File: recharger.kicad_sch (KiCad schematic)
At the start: 22 parts, among them J1 USB_C_Receptacle_USB2.0_14P, J3 Conn_01x03, U2 BQ25886RGE, U3 TPD2EUSB30

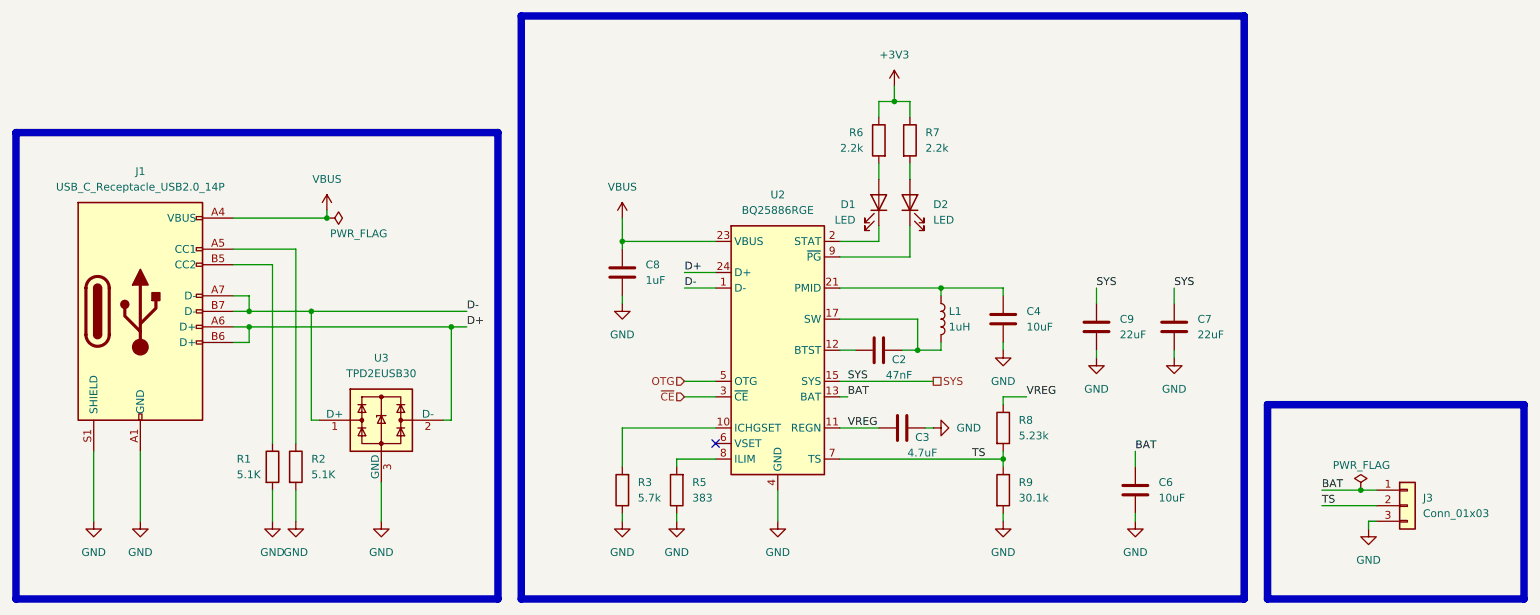
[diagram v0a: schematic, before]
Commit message: update schematic
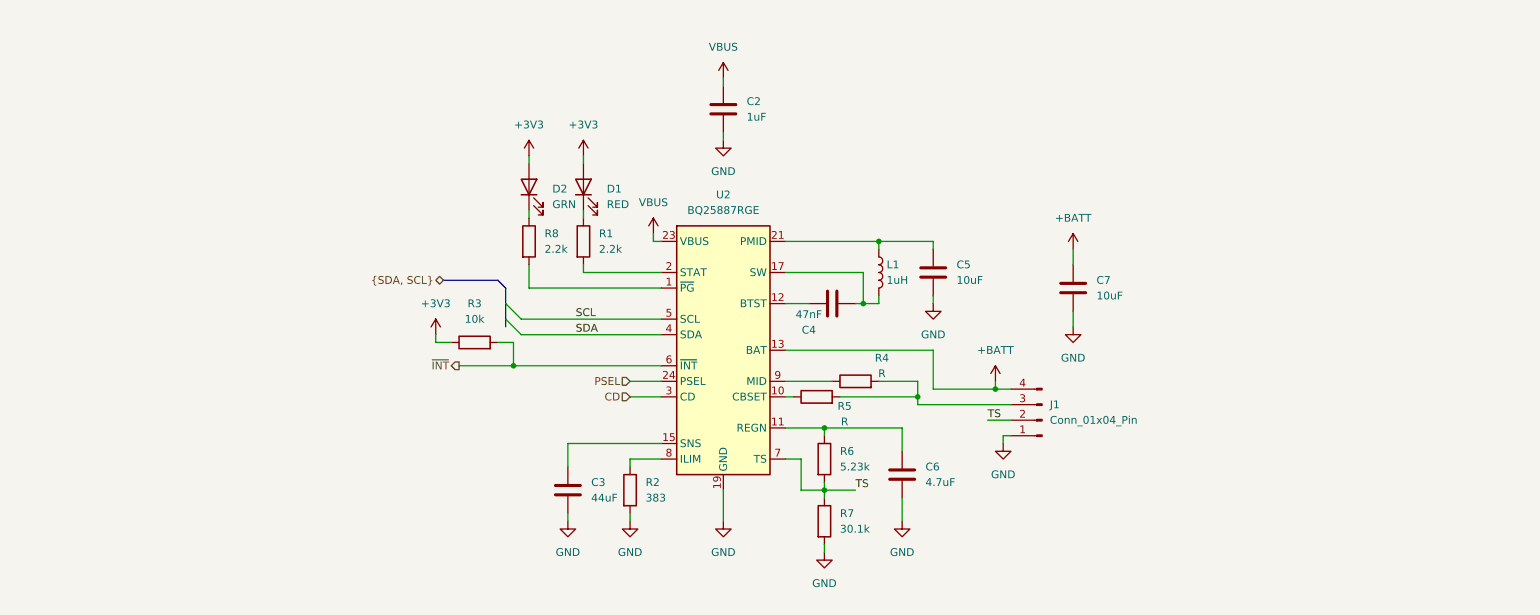
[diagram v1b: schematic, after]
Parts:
- removed C8: 1uF, Capacitor_SMD:C_0402_1005Metric, symbol Device:C
- removed C9: 22uF, Capacitor_SMD:C_1210_3225Metric, symbol Device:C
- removed J1: USB_C_Receptacle_USB2.0_14P, Connector_USB:USB_C_Receptacle_G-Switch_GT-USB-7010ASV, symbol Connector:USB_C_Receptacle_USB2.0_14P
- removed J3: Conn_01x03, symbol Connector_Generic:Conn_01x03
- removed R9: 30.1k, symbol Device:R
- removed U2: BQ25886RGE, Package_DFN_QFN:Texas_RGE0024H_VQFN-24-1EP_4x4mm_P0.5mm_EP2.7x2.7mm, symbol Battery_Management:BQ25886RGE
- removed U3: TPD2EUSB30, Package_TO_SOT_SMD:Texas_DRT-3, symbol Power_Protection:TPD2EUSB30
- added C5: 10uF, symbol Device:C
- added J1: Conn_01x04_Pin, symbol Connector:Conn_01x04_Pin
- added R4: R, symbol Device:R
- added U2: BQ25887RGE, Package_DFN_QFN:Texas_RGE0024H_VQFN-24-1EP_4x4mm_P0.5mm_EP2.7x2.7mm, symbol Battery_Management:BQ25887RGE
- C2: value 47nF -> 1uF; footprint Capacitor_SMD:C_0402_1005Metric -> (none)
- C3: value 4.7uF -> 44uF; footprint Capacitor_SMD:C_0603_1608Metric -> (none)
- C4: value 10uF -> 47nF; footprint Capacitor_SMD:C_0603_1608Metric -> (none)
- C6: value 10uF -> 4.7uF; footprint Capacitor_SMD:C_0805_2012Metric -> (none)
- C7: value 22uF -> 10uF; footprint Capacitor_SMD:C_1210_3225Metric -> (none)
- D1: value LED -> RED
- D2: value LED -> GRN
- L1: footprint Inductor_SMD:L_1008_2520Metric -> (none)
- R1: value 5.1K -> 2.2k; footprint Resistor_SMD:R_0805_2012Metric -> (none); LCSC C27834 -> (none)
- R2: value 5.1K -> 383; footprint Resistor_SMD:R_0805_2012Metric -> (none); LCSC C27834 -> (none)
- R3: value 5.7k -> 10k
- R5: value 383 -> R
- R6: value 2.2k -> 5.23k
- R7: value 2.2k -> 30.1k
- R8: value 5.23k -> 2.2k
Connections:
- net +3V3: now also D1.2 (A), D2.2 (A), R3.1; no longer R6.1, R7.1
- net GND: now also C2.2, R7.2, C5.2, J1.1 (Pin_1), U2.19 (GND), U2.20 (GND), U2.25 (GND); no longer C4.2, R1.2, R3.1, R5.1
- net TS: now also R6.2, R7.1, J1.2 (Pin_2), U2.7 (TS); no longer R8.2
- net VBUS: now also C2.1, U2.23 (VBUS)
- net ~{INT}: now reaches R3.2
- net ~{INT}: now also U2.6 (~{INT})
- net at L1.2: now also C4.1, U2.17 (SW), U2.18 (SW); no longer C2.2
- net at D1.1 (K): now also R1.1
- net at L1.1: now also C5.1, U2.21 (PMID), U2.22 (PMID); no longer C4.1
- net at R5.2: now also J1.3 (Pin_3), R4.2
- net at D2.1 (K): now also R8.1
- net at R2.1: now also U2.8 (ILIM)
- net BAT: no longer names the net of C6.1
- net BAT: now also R6.1, U2.11 (REGN)
- net SYS renamed +BATT
- net +BATT: now also J1.4 (Pin_4), U2.13 (BAT), U2.14 (BAT)
- net VREG: no longer names the net of C3.1
- net VREG: now also U2.15 (SNS), U2.16 (SNS); no longer R8.1
- new net: R1.2, U2.2 (STAT)
- new net: R8.2, U2.1 (~{PG})
- new net: R5.1, U2.10 (CBSET)
- new net: C4.2, U2.12 (BTST)
- new net: R4.1, U2.9 (MID)
- new net CD: U2.3 (CD)
- new net PSEL: U2.24 (PSEL)
- new net SCL: U2.5 (SCL)
- new net SDA: U2.4 (SDA)
- no-connect marks 1 -> 0

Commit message: improve design
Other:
- title: (none) -> Dropbot
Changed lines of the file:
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@@
 	(generator_version "10.0")
 	(paper "A4")
+	(title_block
+		(title "Dropbot")
+	)
 	(junction
 		(at 186.69 105.41)

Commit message: moving on routing
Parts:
- added C12: 22uF, Capacitor_SMD:C_1206_3216Metric, symbol Device:C
- C2, C4, C6: footprint (none) -> Capacitor_SMD:C_0603_1608Metric
- C3: value 44uF -> 22uF; footprint (none) -> Capacitor_SMD:C_1206_3216Metric
- C5: footprint (none) -> Capacitor_SMD:C_1206_3216Metric
- C7: footprint (none) -> Capacitor_SMD:C_0805_2012Metric
- D1, D2: footprint (none) -> LED_SMD:LED_0603_1608Metric
- J1: value Conn_01x04_Pin -> Battery Connector; footprint (none) -> Connector_JST:JST_PH_S4B-PH-K_1x04_P2.00mm_Horizontal
- L1: footprint (none) -> Inductor_SMD:L_1008_2520Metric
- R1, R3, R6, R7, R8: footprint (none) -> Resistor_SMD:R_0603_1608Metric
- R2: value 383 -> 1.1K; footprint (none) -> Resistor_SMD:R_0603_1608Metric
- R4: value R -> 300; footprint (none) -> Resistor_SMD:R_0603_1608Metric
- R5: footprint (none) -> Resistor_SMD:R_2512_6332Metric
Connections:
- net +3V3: no longer D1.2 (A), D2.2 (A)
- net GND: now also C12.2
- net at C3.1, U2.15 (SNS), U2.16 (SNS): now also C12.1
- net REGN: now reaches C6.1, R6.1, U2.11 (REGN)
- net REGN: now also D1.2 (A), D2.2 (A)
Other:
- moved on the sheet: C7

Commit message: update PCB
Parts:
- J1: footprint Connector_JST:JST_PH_S4B-PH-K_1x04_P2.00mm_Horizontal -> Connector_JST:JST_PH_S4B-PH-SM4-TB_1x04-1MP_P2.00mm_Horizontal
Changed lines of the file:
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@@
 			)
 		)
-		(property "Footprint" "Connector_JST:JST_PH_S4B-PH-K_1x04_P2.00mm_Horizontal"
+		(property "Footprint" "Connector_JST:JST_PH_S4B-PH-SM4-TB_1x04-1MP_P2.00mm_Horizontal"
 			(at 194.31 110.49 0)
 			(hide yes)

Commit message: more on layout
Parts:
- R5: value R -> 10
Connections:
- net CBSET_PIN: now reaches J1.3 (Pin_3), R4.2, R5.2
- net CBSET_IN: now reaches R5.1, U2.10 (CBSET)
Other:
- moved on the sheet: J1, R4, R5
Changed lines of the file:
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@@
 	)
 	(junction
-		(at 186.69 105.41)
+		(at 186.69 104.14)
 		(diameter 0)
 		(color 0 0 0 0)
@@
 	)
 	(junction
-		(at 173.99 106.68)
+		(at 158.75 121.92)
 		(diameter 0)
 		(color 0 0 0 0)
@@
 	)
 	(junction
-		(at 158.75 121.92)
+		(at 173.99 106.68)
 		(diameter 0)
 		(color 0 0 0 0)
@@
 	(wire
 		(pts
-			(xy 186.69 104.14) (xy 186.69 105.41)
+			(xy 186.69 102.87) (xy 186.69 104.14)
 		)
 		(stroke
@@
 	(wire
 		(pts
-			(xy 176.53 99.06) (xy 176.53 105.41)
+			(xy 176.53 99.06) (xy 176.53 104.14)
 		)
 		(stroke
@@
 	(wire
 		(pts
-			(xy 161.29 106.68) (xy 173.99 106.68)
+			(xy 163.83 106.68) (xy 173.99 106.68)
 		)
 		(stroke
@@
 	(wire
 		(pts
-			(xy 185.42 110.49) (xy 189.23 110.49)
+			(xy 185.42 109.22) (xy 189.23 109.22)
 		)
 		(stroke
@@
 	(wire
 		(pts
-			(xy 173.99 104.14) (xy 167.64 104.14)
+			(xy 173.99 104.14) (xy 170.18 104.14)
 		)
 		(stroke
@@
 	(wire
 		(pts
-			(xy 187.96 113.03) (xy 189.23 113.03)
+			(xy 187.96 111.76) (xy 189.23 111.76)
 		)
 		(stroke
@@
 	(wire
 		(pts
-			(xy 173.99 107.95) (xy 189.23 107.95)
+			(xy 173.99 106.68) (xy 189.23 106.68)
 		)
 		(stroke
@@
 	(wire
 		(pts
-			(xy 187.96 113.03) (xy 187.96 114.3)
+			(xy 187.96 111.76) (xy 187.96 113.03)
 		)
 		(stroke
@@
 	(wire
 		(pts
-			(xy 152.4 106.68) (xy 153.67 106.68)
+			(xy 152.4 106.68) (xy 156.21 106.68)
 		)
 		(stroke
@@
 	(wire
 		(pts
-			(xy 186.69 105.41) (xy 189.23 105.41)
+			(xy 186.69 104.14) (xy 189.23 104.14)
 		)
 		(stroke
@@
 	(wire
 		(pts
-			(xy 152.4 104.14) (xy 160.02 104.14)
+			(xy 152.4 104.14) (xy 162.56 104.14)
 		)
 		(stroke
@@
 	(wire
 		(pts
-			(xy 176.53 105.41) (xy 186.69 105.41)
+			(xy 176.53 104.14) (xy 186.69 104.14)
 		)
 		(stroke
@@
 	(wire
 		(pts
-			(xy 173.99 106.68) (xy 173.99 107.95)
-		)
-		(stroke
-			(width 0)
-			(type default)
-		)
-	)
-	(wire
-		(pts
 			(xy 127 106.68) (xy 132.08 106.68)
 		)
@@
 		)
 	)
+	(label "CBSET_IN"
+		(at 152.4 106.68 0)
+		(effects
+			(font
+				(size 0.508 0.508)
+			)
+			(justify left bottom)
+		)
+	)
 	(label "SCL"
 		(at 118.11 93.98 0)
@@
 		)
 	)
+	(label "CBSET_PIN"
+		(at 166.37 106.68 0)
+		(effects
+			(font
+				(size 0.508 0.508)
+			)
+			(justify left bottom)
+		)
+	)
 	(label "REGN"
 		(at 119.38 67.31 0)
@@
 	)
 	(label "TS"
-		(at 185.42 110.49 0)
+		(at 185.42 109.22 0)
 		(effects
 			(font
@@
 	)
 	(label "REGN"
-		(at 171.45 111.76 0)
+		(at 171.45 114.3 0)
 		(effects
 			(font
@@
 	(symbol
 		(lib_id "Connector:Conn_01x04_Pin")
-		(at 194.31 110.49 180)
+		(at 194.31 109.22 180)
 		(unit 1)
 		(body_style 1)
@@
 		(fields_autoplaced yes)
 		(property "Reference" "J1"
-			(at 195.58 107.9499 0)
+			(at 195.58 106.6799 0)
 			(show_name no)
 			(do_not_autoplace no)
@@
 		)
 		(property "Value" "Battery Connector"
-			(at 195.58 110.4899 0)
+			(at 195.58 109.2199 0)
 			(show_name no)
 			(do_not_autoplace no)
@@
 		)
 		(property "Footprint" "Connector_JST:JST_PH_S4B-PH-SM4-TB_1x04-1MP_P2.00mm_Horizontal"
-			(at 194.31 110.49 0)
+			(at 194.31 109.22 0)
 			(hide yes)
 			(show_name no)
@@
 		)
 		(property "Datasheet" ""
-			(at 194.31 110.49 0)
+			(at 194.31 109.22 0)
 			(hide yes)
 			(show_name no)
@@
 		)
 		(property "Description" "Generic connector, single row, 01x04, script generated"
-			(at 194.31 110.49 0)
+			(at 194.31 109.22 0)
 			(hide yes)
 			(show_name no)
@@
 	(symbol
 		(lib_id "power:GND")
-		(at 187.96 114.3 0)
+		(at 187.96 113.03 0)
 		(unit 1)
 		(body_style 1)
@@
 		(fields_autoplaced yes)
 		(property "Reference" "#PWR015"
-			(at 187.96 120.65 0)
+			(at 187.96 119.38 0)
 			(hide yes)
 			(show_name no)
@@
 		)
 		(property "Value" "GND"
-			(at 187.96 119.38 0)
+			(at 187.96 118.11 0)
 			(show_name no)
 			(do_not_autoplace no)
@@
 		)
 		(property "Footprint" ""
-			(at 187.96 114.3 0)
+			(at 187.96 113.03 0)
 			(hide yes)
 			(show_name no)
@@
 		)
 		(property "Datasheet" ""
-			(at 187.96 114.3 0)
+			(at 187.96 113.03 0)
 			(hide yes)
 			(show_name no)
@@
 		)
 		(property "Description" "Power symbol creates a global label with name \"GND\" , ground"
-			(at 187.96 114.3 0)
+			(at 187.96 113.03 0)
 			(hide yes)
 			(show_name no)
@@
 	(symbol
 		(lib_id "power:+BATT")
-		(at 186.69 104.14 0)
+		(at 186.69 102.87 0)
 		(unit 1)
 		(body_style 1)
@@
 		(fields_autoplaced yes)
 		(property "Reference" "#PWR018"
-			(at 186.69 107.95 0)
+			(at 186.69 106.68 0)
 			(hide yes)
 			(show_name no)
@@
 		)
 		(property "Value" "+BATT"
-			(at 186.69 99.06 0)
+			(at 186.69 97.79 0)
 			(show_name no)
 			(do_not_autoplace no)
@@
 		)
 		(property "Footprint" ""
-			(at 186.69 104.14 0)
+			(at 186.69 102.87 0)
 			(hide yes)
 			(show_name no)
@@
 		)
 		(property "Datasheet" ""
-			(at 186.69 104.14 0)
+			(at 186.69 102.87 0)
 			(hide yes)
 			(show_name no)
@@
 		)
 		(property "Description" "Power symbol creates a global label with name \"+BATT\""
-			(at 186.69 104.14 0)
+			(at 186.69 102.87 0)
 			(hide yes)
 			(show_name no)
@@
 	(symbol
 		(lib_id "Device:R")
-		(at 157.48 106.68 90)
+		(at 160.02 106.68 90)
 		(unit 1)
 		(body_style 1)
@@
 		(dnp no)
 		(property "Reference" "R5"
-			(at 162.052 108.204 90)
+			(at 164.592 108.204 90)
 			(show_name no)
 			(do_not_autoplace no)
@@
 			)
 		)
-		(property "Value" "R"
-			(at 162.052 110.744 90)
+		(property "Value" "10"
+			(at 164.592 110.744 90)
 			(show_name no)
 			(do_not_autoplace no)
@@
 		)
 		(property "Footprint" "Resistor_SMD:R_2512_6332Metric"
-			(at 157.48 108.458 90)
+			(at 160.02 108.458 90)
 			(hide yes)
 			(show_name no)
@@
 		)
 		(property "Datasheet" ""
-			(at 157.48 106.68 0)
+			(at 160.02 106.68 0)
 			(hide yes)
 			(show_name no)
@@
 		)
 		(property "Description" "Resistor"
-			(at 157.48 106.68 0)
+			(at 160.02 106.68 0)
 			(hide yes)
 			(show_name no)
@@
 	(symbol
 		(lib_id "Device:R")
-		(at 163.83 104.14 90)
+		(at 166.37 104.14 90)
 		(unit 1)
 		(body_style 1)
@@
 		(dnp no)
 		(property "Reference" "R4"
-			(at 168.148 100.33 90)
+			(at 171.704 100.33 90)
 			(show_name no)
 			(do_not_autoplace no)
@@
 		)
 		(property "Value" "300"
-			(at 168.148 102.87 90)
+			(at 171.704 102.87 90)
 			(show_name no)
 			(do_not_autoplace no)
@@
 		)
 		(property "Footprint" "Resistor_SMD:R_0603_1608Metric"
-			(at 163.83 105.918 90)
+			(at 166.37 105.918 90)
 			(hide yes)
 			(show_name no)
@@
 		)
 		(property "Datasheet" ""
-			(at 163.83 104.14 0)
+			(at 166.37 104.14 0)
 			(hide yes)
 			(show_name no)
@@
 		)
 		(property "Description" "Resistor"
-			(at 163.83 104.14 0)
+			(at 166.37 104.14 0)
 			(hide yes)
 			(show_name no)

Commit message: updates
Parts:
- L1: footprint Inductor_SMD:L_1008_2520Metric -> Inductor_SMD:L_Sunlord_MWSA0518S
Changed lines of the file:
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@@
 			)
 		)
-		(property "Footprint" "Inductor_SMD:L_1008_2520Metric"
+		(property "Footprint" "Inductor_SMD:L_Sunlord_MWSA0518S"
 			(at 167.64 86.36 0)
 			(hide yes)

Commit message: progress on routing
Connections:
- net +3V3 is gone; now on net REGN: R3.1
- net CD: no longer names the net of U2.3 (CD)
- net PSEL: no longer names the net of U2.24 (PSEL)
- net ~{INT}: no longer names the net of R3.2, U2.6 (~{INT})
- no-connect marks 0 -> 1
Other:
- moved on the sheet: R3
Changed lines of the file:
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@@
-	)
-	(junction
-		(at 107.95 101.6)
-		(diameter 0)
-		(color 0 0 0 0)
 	)
 	(junction
@@
 		(color 0 0 0 0)
 	)
+	(no_connect
+		(at 132.08 104.14)
+	)
 	(bus_entry
 		(at 106.68 93.98)
@@
 	(wire
 		(pts
-			(xy 95.25 97.79) (xy 97.79 97.79)
+			(xy 93.98 101.6) (xy 100.33 101.6)
 		)
 		(stroke
@@
 	(wire
 		(pts
-			(xy 107.95 97.79) (xy 107.95 101.6)
-		)
-		(stroke
-			(width 0)
-			(type default)
-		)
-	)
-	(wire
-		(pts
 			(xy 158.75 120.65) (xy 158.75 121.92)
 		)
@@
 	(wire
 		(pts
-			(xy 99.06 101.6) (xy 107.95 101.6)
-		)
-		(stroke
-			(width 0)
-			(type default)
-		)
-	)
-	(wire
-		(pts
 			(xy 142.24 121.92) (xy 142.24 127)
 		)
@@
 	(wire
 		(pts
+			(xy 187.96 111.76) (xy 187.96 113.03)
+		)
+		(stroke
+			(width 0)
+			(type default)
+		)
+	)
+	(wire
+		(pts
+			(xy 105.41 114.3) (xy 116.84 114.3)
+		)
+		(stroke
+			(width 0)
+			(type default)
+		)
+	)
+	(bus
+		(pts
+			(xy 106.68 93.98) (xy 106.68 95.25)
+		)
+		(stroke
+			(width 0)
+			(type default)
+		)
+	)
+	(wire
+		(pts
+			(xy 158.75 111.76) (xy 158.75 113.03)
+		)
+		(stroke
+			(width 0)
+			(type default)
+		)
+	)
+	(wire
+		(pts
+			(xy 173.99 104.14) (xy 173.99 106.68)
+		)
+		(stroke
+			(width 0)
+			(type default)
+		)
+	)
+	(wire
+		(pts
+			(xy 152.4 106.68) (xy 156.21 106.68)
+		)
+		(stroke
+			(width 0)
+			(type default)
+		)
+	)
+	(wire
+		(pts
+			(xy 207.01 80.01) (xy 207.01 82.55)
+		)
+		(stroke
+			(width 0)
+			(type default)
+		)
+	)
+	(wire
+		(pts
 			(xy 107.95 101.6) (xy 132.08 101.6)
 		)
@@
 	(wire
 		(pts
-			(xy 187.96 111.76) (xy 187.96 113.03)
-		)
-		(stroke
-			(width 0)
-			(type default)
-		)
-	)
-	(wire
-		(pts
-			(xy 105.41 114.3) (xy 116.84 114.3)
-		)
-		(stroke
-			(width 0)
-			(type default)
-		)
-	)
-	(bus
-		(pts
-			(xy 106.68 93.98) (xy 106.68 95.25)
-		)
-		(stroke
-			(width 0)
-			(type default)
-		)
-	)
-	(wire
-		(pts
-			(xy 158.75 111.76) (xy 158.75 113.03)
-		)
-		(stroke
-			(width 0)
-			(type default)
-		)
-	)
-	(wire
-		(pts
-			(xy 173.99 104.14) (xy 173.99 106.68)
-		)
-		(stroke
-			(width 0)
-			(type default)
-		)
-	)
-	(wire
-		(pts
-			(xy 95.25 96.52) (xy 95.25 97.79)
-		)
-		(stroke
-			(width 0)
-			(type default)
-		)
-	)
-	(wire
-		(pts
-			(xy 152.4 106.68) (xy 156.21 106.68)
-		)
-		(stroke
-			(width 0)
-			(type default)
-		)
-	)
-	(wire
-		(pts
-			(xy 207.01 80.01) (xy 207.01 82.55)
-		)
-		(stroke
-			(width 0)
-			(type default)
-		)
-	)
-	(wire
-		(pts
-			(xy 107.95 97.79) (xy 105.41 97.79)
-		)
-		(stroke
-			(width 0)
-			(type default)
-		)
-	)
-	(wire
-		(pts
 			(xy 176.53 81.28) (xy 176.53 82.55)
 		)
@@
 	(wire
 		(pts
-			(xy 127 104.14) (xy 132.08 104.14)
-		)
-		(stroke
-			(width 0)
-			(type default)
-		)
-	)
-	(wire
-		(pts
 			(xy 207.01 90.17) (xy 207.01 92.71)
 		)
@@
 		(pts
 			(xy 171.45 111.76) (xy 171.45 115.57)
-		)
-		(stroke
-			(width 0)
-			(type default)
-		)
-	)
-	(wire
-		(pts
-			(xy 127 106.68) (xy 132.08 106.68)
 		)
 		(stroke
@@
 		)
 	)
+	(label "REGN"
+		(at 93.98 101.6 0)
+		(effects
+			(font
+				(size 1.27 1.27)
+			)
+			(justify left bottom)
+		)
+	)
 	(label "TS"
 		(at 163.83 121.92 0)
@@
 			)
 			(justify left bottom)
-		)
-	)
-	(hierarchical_label "CD"
-		(shape input)
-		(at 127 106.68 180)
-		(effects
-			(font
-				(size 1.27 1.27)
-			)
-			(justify right)
-		)
-	)
-	(hierarchical_label "PSEL"
-		(shape input)
-		(at 127 104.14 180)
-		(effects
-			(font
-				(size 1.27 1.27)
-			)
-			(justify right)
 		)
 	)
@@
 		(shape bidirectional)
 		(at 96.52 87.63 180)
-		(effects
-			(font
-				(size 1.27 1.27)
-			)
-			(justify right)
-		)
-	)
-	(hierarchical_label "~{INT}"
-		(shape output)
-		(at 99.06 101.6 180)
 		(effects
 			(font
@@
 	(symbol
 		(lib_id "Device:R")
-		(at 101.6 97.79 90)
+		(at 104.14 101.6 90)
 		(unit 1)
 		(body_style 1)
@@
 		(fields_autoplaced yes)
 		(property "Reference" "R3"
-			(at 101.6 91.44 90)
+			(at 104.14 95.25 90)
 			(show_name no)
 			(do_not_autoplace no)
@@
 		)
 		(property "Value" "10k"
-			(at 101.6 93.98 90)
+			(at 104.14 97.79 90)
 			(show_name no)
 			(do_not_autoplace no)
@@
 		)
 		(property "Footprint" "Resistor_SMD:R_0603_1608Metric"
-			(at 101.6 99.568 90)
+			(at 104.14 103.378 90)
 			(hide yes)
 			(show_name no)
@@
 		)
 		(property "Datasheet" ""
-			(at 101.6 97.79 0)
+			(at 104.14 101.6 0)
 			(hide yes)
 			(show_name no)
@@
 		)
 		(property "Description" "Resistor"
-			(at 101.6 97.79 0)
+			(at 104.14 101.6 0)
 			(hide yes)
 			(show_name no)
@@
 					(unit 1)
 				)
-			)
-		)
-	)
-	(symbol
-		(lib_id "power:+3V3")
-		(at 95.25 96.52 0)
-		(unit 1)
-		(body_style 1)
-		(exclude_from_sim no)
-		(in_bom yes)
-		(on_board yes)
-		(in_pos_files yes)
-		(dnp no)
-		(fields_autoplaced yes)
-		(property "Reference" "#PWR013"
-			(at 95.25 100.33 0)
-			(hide yes)
-			(show_name no)
-			(do_not_autoplace no)
-			(effects
-				(font
-					(size 1.27 1.27)
-				)
-			)
-		)
-		(property "Value" "+3V3"
-			(at 95.25 91.44 0)
-			(show_name no)
-			(do_not_autoplace no)
-			(effects
-				(font
-					(size 1.27 1.27)
-				)
-			)
-		)
-		(property "Footprint" ""
-			(at 95.25 96.52 0)
-			(hide yes)
-			(show_name no)
-			(do_not_autoplace no)
-			(effects
-				(font
-					(size 1.27 1.27)
-				)
-			)
-		)
-		(property "Datasheet" ""
-			(at 95.25 96.52 0)
-			(hide yes)
-			(show_name no)
-			(do_not_autoplace no)
-			(effects
-				(font
-					(size 1.27 1.27)
-				)
-			)
-		)
-		(property "Description" "Power symbol creates a global label with name \"+3V3\""
-			(at 95.25 96.52 0)
-			(hide yes)
-			(show_name no)
-			(do_not_autoplace no)
-			(effects
-				(font
-					(size 1.27 1.27)
-				)
-			)
-		)
-		(pin "1"
-		)
-		(instances
-			(project "rover-circuit"
-				(path "/0461baee-3b25-4e1a-a5c1-d76b4b99c66c/d12ae2b7-4c48-4e18-8e74-760d158fba59"
-					(reference "#PWR013")
-					(unit 1)
-				)

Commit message: complete routing and validated ERC/DRC
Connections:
- no-connect marks 1 -> 2
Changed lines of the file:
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@@
+	)
+	(no_connect
+		(at 132.08 106.68)
 	)
 	(no_connect
